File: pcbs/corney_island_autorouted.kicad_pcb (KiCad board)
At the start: 2 copper layers, 133.8 x 91.7 mm, 101 parts

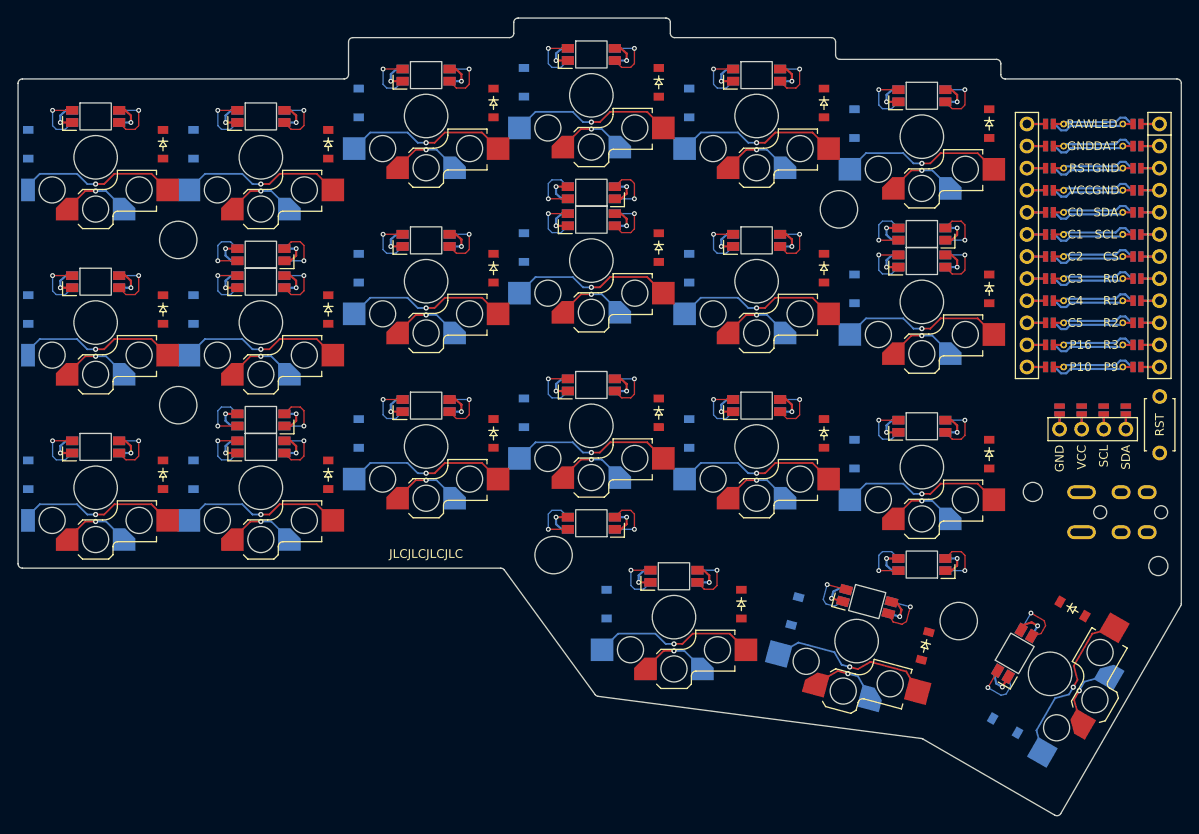
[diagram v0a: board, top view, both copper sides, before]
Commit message: build: generate PCB layouts, routing, gerbers, and preview images
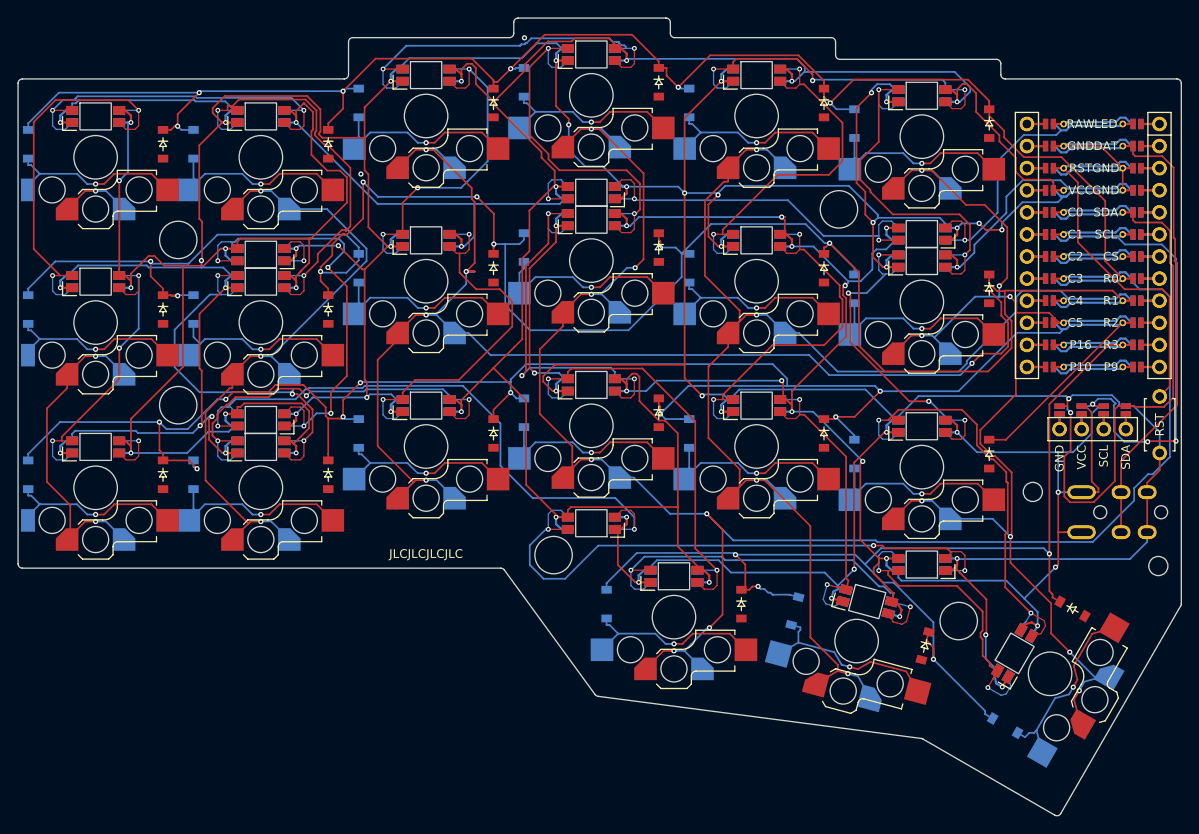
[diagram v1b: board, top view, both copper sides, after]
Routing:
- net GND: track 130.3 -> 697.8 mm, vias 27 -> 44
- net VCC: track 111.0 -> 672.8 mm, vias 27 -> 34
- net R1: track 9.63 -> 232.3 mm, vias 0 -> 8
- net R2: track 9.63 -> 221.9 mm, vias 0 -> 9
- net R0: track 9.63 -> 190.1 mm, vias 0 -> 6
- net C3: track 42.7 -> 201.7 mm, vias 4 -> 7
- net R3: track 9.63 -> 139.1 mm, vias 0 -> 4
- net C2: track 34.5 -> 157.1 mm, vias 3 -> 5
- net C4: track 42.7 -> 150.0 mm
- net C5: track 42.7 -> 139.9 mm, vias 4 -> 8
- net SDA: track 9.63 -> 69.4 mm, vias 0 -> 1
- net ULED_4: track 13.5 -> 72.0 mm
- net ULED_5: track 13.5 -> 69.7 mm, vias 2 -> 3
- net DAT: track 9.63 -> 61.3 mm
- net C1: track 34.5 -> 83.1 mm
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
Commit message: build: regenerate PCBs, images, and gerbers
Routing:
- net VCC: track 672.8 -> 489.8 mm, vias 34 -> 29
- net GND: track 697.8 -> 559.2 mm, vias 44 -> 35
- net C1: track 83.1 -> 198.4 mm, vias 3 -> 4
- net C4: track 150.0 -> 50.6 mm, vias 4 -> 5
- net ULED_5: track 69.7 -> 13.5 mm, vias 3 -> 2
- net LED_17: track 48.7 -> 13.5 mm
- net RST: track 44.3 -> 9.96 mm
- net LED_16: track 47.4 -> 13.5 mm, vias 3 -> 2
- net LED_8: track 47.2 -> 13.5 mm
- net LED_19: track 46.1 -> 13.5 mm
- net ULED_2: track 13.5 -> 44.0 mm
- net LED_3: track 43.4 -> 13.5 mm
- net LED_14: track 42.6 -> 13.5 mm
- net R0: track 190.1 -> 216.6 mm, vias 6 -> 8
- net C2: track 157.1 -> 181.8 mm, vias 5 -> 6
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
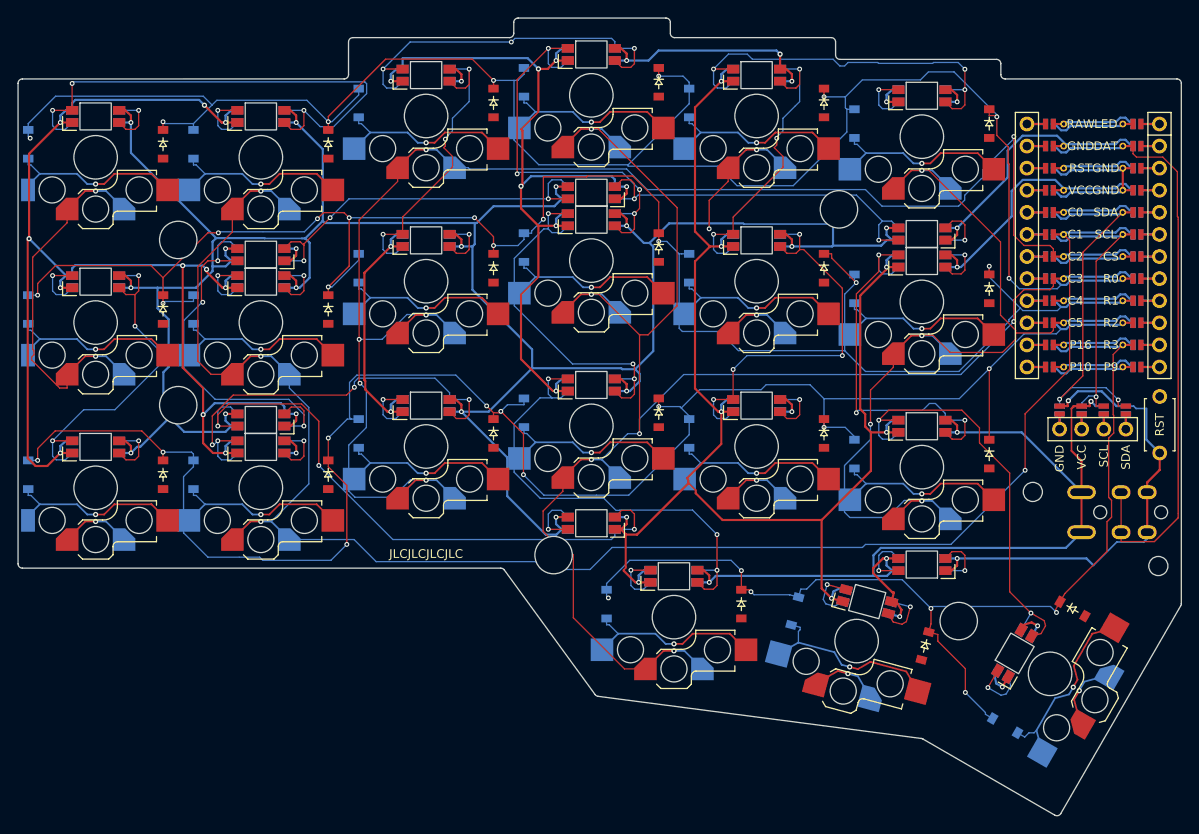
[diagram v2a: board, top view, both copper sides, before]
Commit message: fix(build): restore NPTH normalization and regenerate boards
Normalize source-proven NPTH export obstacles by default, with a native-export opt-out. Pin and verify Freerouting 2.5.1-SNAPSHOT at upstream head 1be66ad and use KiCad 9 for generation, import, and DRC. Make CI run the same build and withhold stale or failing fabrication outputs.

Regenerate the keyboard boards and plates from YAML, including the configured rectangular JST jumpers. Retain routed review boards and unfiltered validation evidence: wireless has one open C4 connection; wired has two open VCC connections. Routing introduces no new KiCad DRC errors. Existing LED clearance and frontplate outline findings remain documented.

Validation: 17 regression tests, actual KiCad 9 export preservation and idempotence checks, post-import DRC, 100 um track-width floor, ShellCheck, shell syntax, workflow YAML validation, and git diff --check.
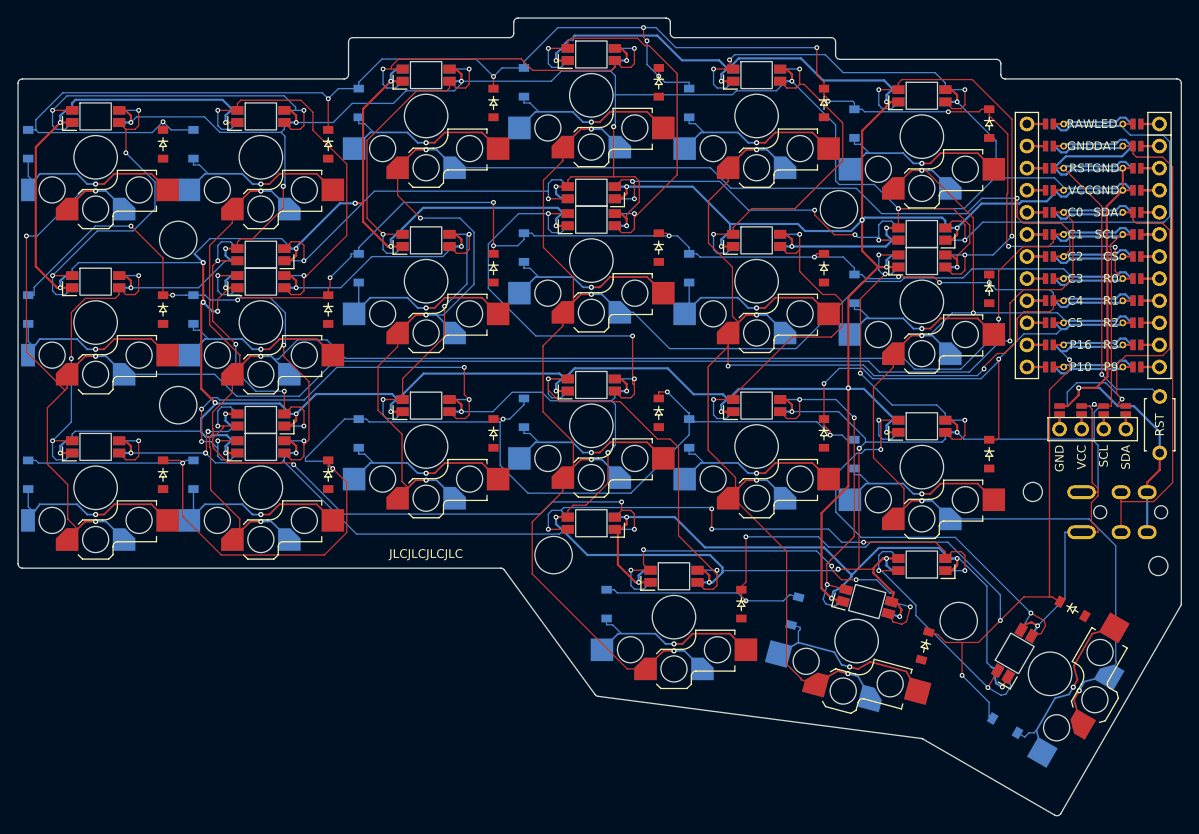
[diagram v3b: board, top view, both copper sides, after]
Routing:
- net C0: track 60.9 -> 211.8 mm, vias 3 -> 5
- net GND: track 559.2 -> 678.4 mm
- net C4: track 50.6 -> 155.9 mm, vias 5 -> 6
- net VCC: track 489.8 -> 591.4 mm, vias 29 -> 35
- net R1: track 210.7 -> 159.1 mm, vias 12 -> 11
- net ULED_5: track 13.5 -> 62.1 mm, vias 2 -> 5
- net LED: track 16.7 -> 56.1 mm
- net LED_3: track 13.5 -> 49.1 mm, vias 2 -> 3
- net LED_8: track 13.5 -> 48.4 mm, vias 2 -> 5
- net RST: track 9.96 -> 43.0 mm, vias 0 -> 1
- net LED_17: track 13.5 -> 46.5 mm
- net LED_7: track 13.5 -> 41.2 mm, vias 2 -> 3
- net LED_19: track 13.5 -> 39.0 mm, vias 2 -> 3
- net LED_16: track 13.5 -> 37.4 mm, vias 2 -> 3
- net LED_14: track 13.5 -> 35.6 mm, vias 2 -> 3
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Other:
- rule pad_to_mask_clearance: 0.05 -> 0

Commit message: Refresh generated Corney Island boards and KiCad projects
Regenerate with KiCad 9.0.7+1 and the Freerouting fixes at 48c969dd, using
neckdown and fanout disabled, one worker, and optimization enabled. The fixed
JAR was mounted over the pinned image for this local build.

Both boards have zero missing connections after SES import. Wireless has no
DRC errors; wired retains the 16 source copper-edge errors. The frontplate
still fails its outline check, so failed-board fabrication exports are skipped.

Regenerate wireless fabrication outputs after the unfiltered KiCad DRC passes,
bypassing KiBot's subsequent HTML-report parsing failure. Include the generated
project settings with the boards, reports, images, and archives.
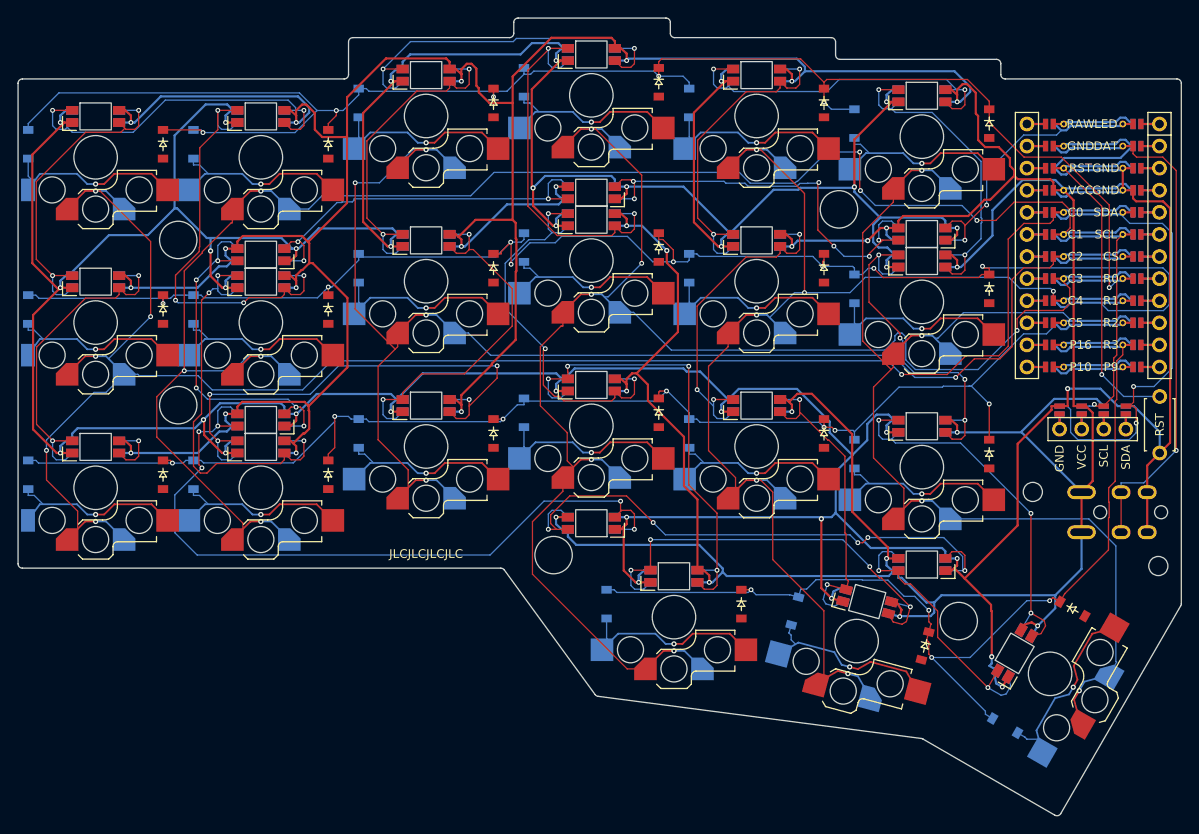
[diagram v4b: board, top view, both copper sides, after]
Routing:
- net VCC: track 591.4 -> 681.9 mm, vias 35 -> 29
- net R2: track 208.4 -> 158.9 mm
- net R1: track 159.1 -> 181.2 mm, vias 11 -> 8
- net LED: track 56.1 -> 34.4 mm, vias 1 -> 2
- net ULED_4: track 68.2 -> 85.1 mm, vias 4 -> 5
- net R3: track 133.7 -> 117.2 mm, vias 5 -> 4
- net GND: track 678.4 -> 692.1 mm, vias 35 -> 34
- net C1: track 178.8 -> 192.4 mm, vias 4 -> 7
- net C3: track 171.1 -> 182.7 mm, vias 4 -> 6
- net LED_3: track 49.1 -> 37.9 mm, vias 3 -> 2
- net C4: track 155.9 -> 144.8 mm
- net LED_1: track 54.9 -> 44.5 mm
- net LED_16: track 37.4 -> 47.6 mm
- net R0: track 206.2 -> 196.8 mm, vias 11 -> 6
- net C2: track 159.9 -> 167.3 mm
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
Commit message: Update LED footprint clearance and refresh generated boards
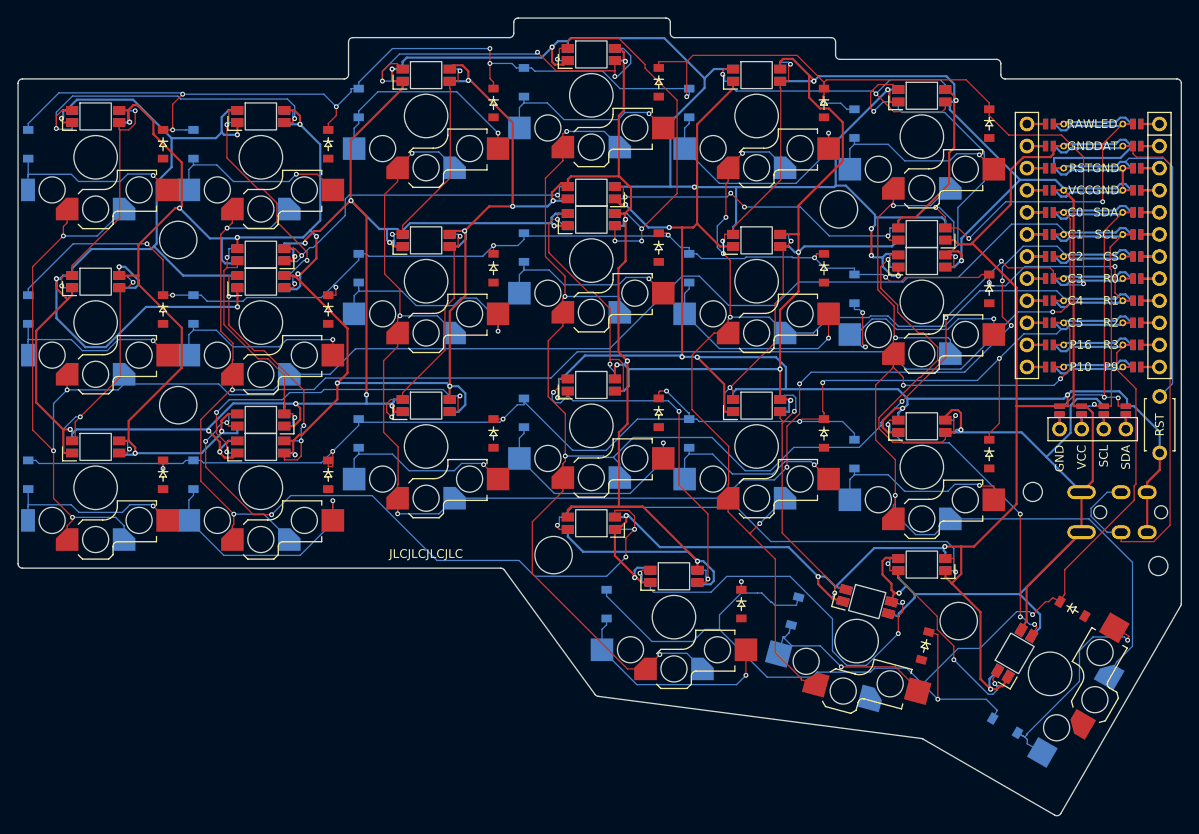
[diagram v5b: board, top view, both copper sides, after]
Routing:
- net GND: track 692.1 -> 781.6 mm
- net R3: track 117.2 -> 142.4 mm, vias 4 -> 3
- net LED_17: track 51.2 -> 30.1 mm, vias 4 -> 3
- net LED_15: track 59.6 -> 40.4 mm, vias 4 -> 3
- net R1: track 181.2 -> 162.6 mm, vias 8 -> 9
- net C1: track 192.4 -> 174.8 mm, vias 7 -> 3
- net SDA: track 56.2 -> 41.1 mm
- net LED_16: track 47.6 -> 32.7 mm
- net LED_10: track 46.3 -> 31.6 mm, vias 3 -> 2
- net LED: track 34.4 -> 48.7 mm, vias 2 -> 3
- net R2: track 158.9 -> 173.1 mm
- net ULED_3: track 41.9 -> 29.2 mm, vias 5 -> 2
- net LED_14: track 41.2 -> 29.1 mm
- net DAT: track 62.1 -> 73.7 mm, vias 1 -> 0
- net ULED_5: track 68.7 -> 57.4 mm, vias 5 -> 2
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
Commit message: Bump version to 0.4 and updated artifacts
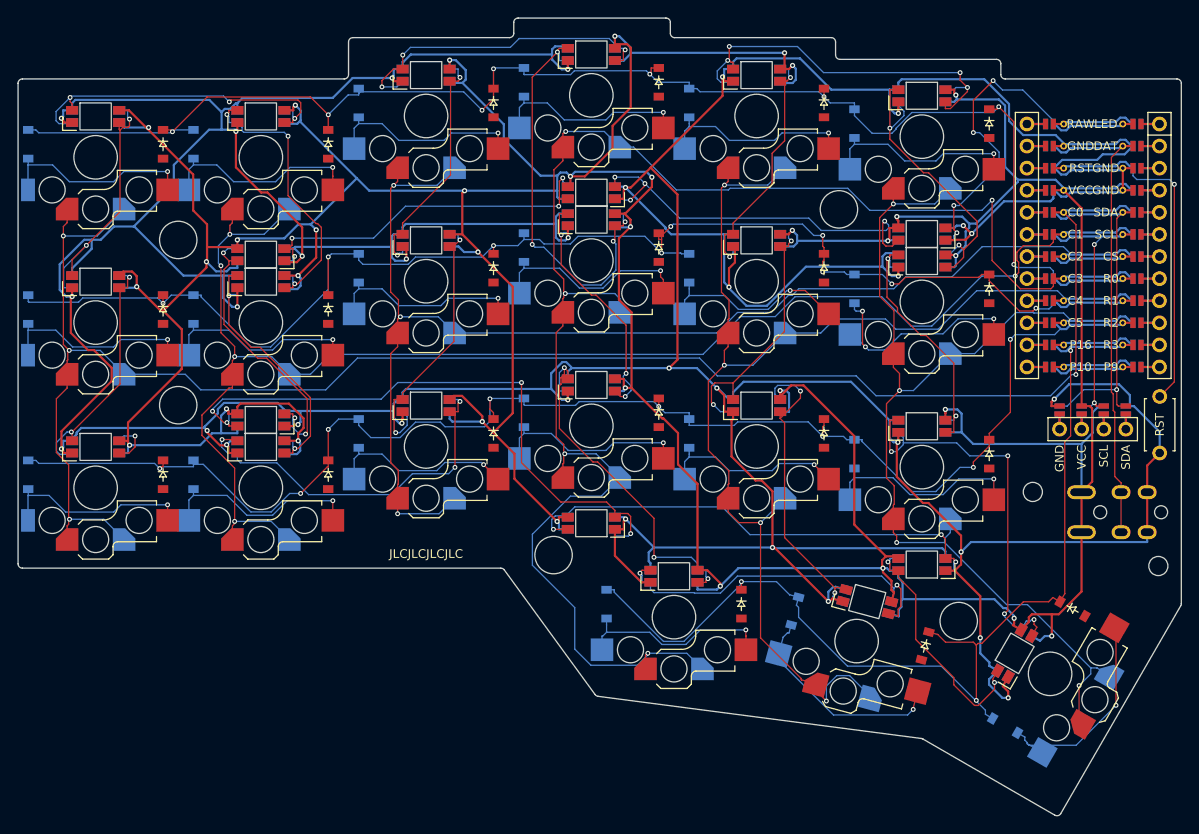
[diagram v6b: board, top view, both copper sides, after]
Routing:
- net GND: track 781.6 -> 758.6 mm, vias 34 -> 32
- net R0: track 193.1 -> 171.1 mm
- net R3: track 142.4 -> 122.9 mm
- net C2: track 167.7 -> 148.8 mm, vias 7 -> 3
- net C5: track 143.9 -> 125.2 mm, vias 5 -> 4
- net DAT: track 73.7 -> 55.2 mm
- net VCC: track 678.1 -> 660.2 mm, vias 29 -> 33
- net LED_2: track 43.0 -> 29.9 mm
- net C4: track 136.0 -> 144.9 mm, vias 5 -> 4
- net LED_1: track 38.7 -> 46.1 mm
- net LED_8: track 48.1 -> 41.0 mm, vias 3 -> 2
- net ULED_1: track 39.6 -> 46.6 mm
- net LED_12: track 43.4 -> 37.6 mm
- net ULED_3: track 29.2 -> 34.3 mm, vias 2 -> 3
- net C0: track 211.2 -> 206.3 mm, vias 5 -> 4
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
